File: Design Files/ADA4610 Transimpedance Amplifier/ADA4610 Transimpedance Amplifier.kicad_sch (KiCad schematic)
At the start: 22 parts

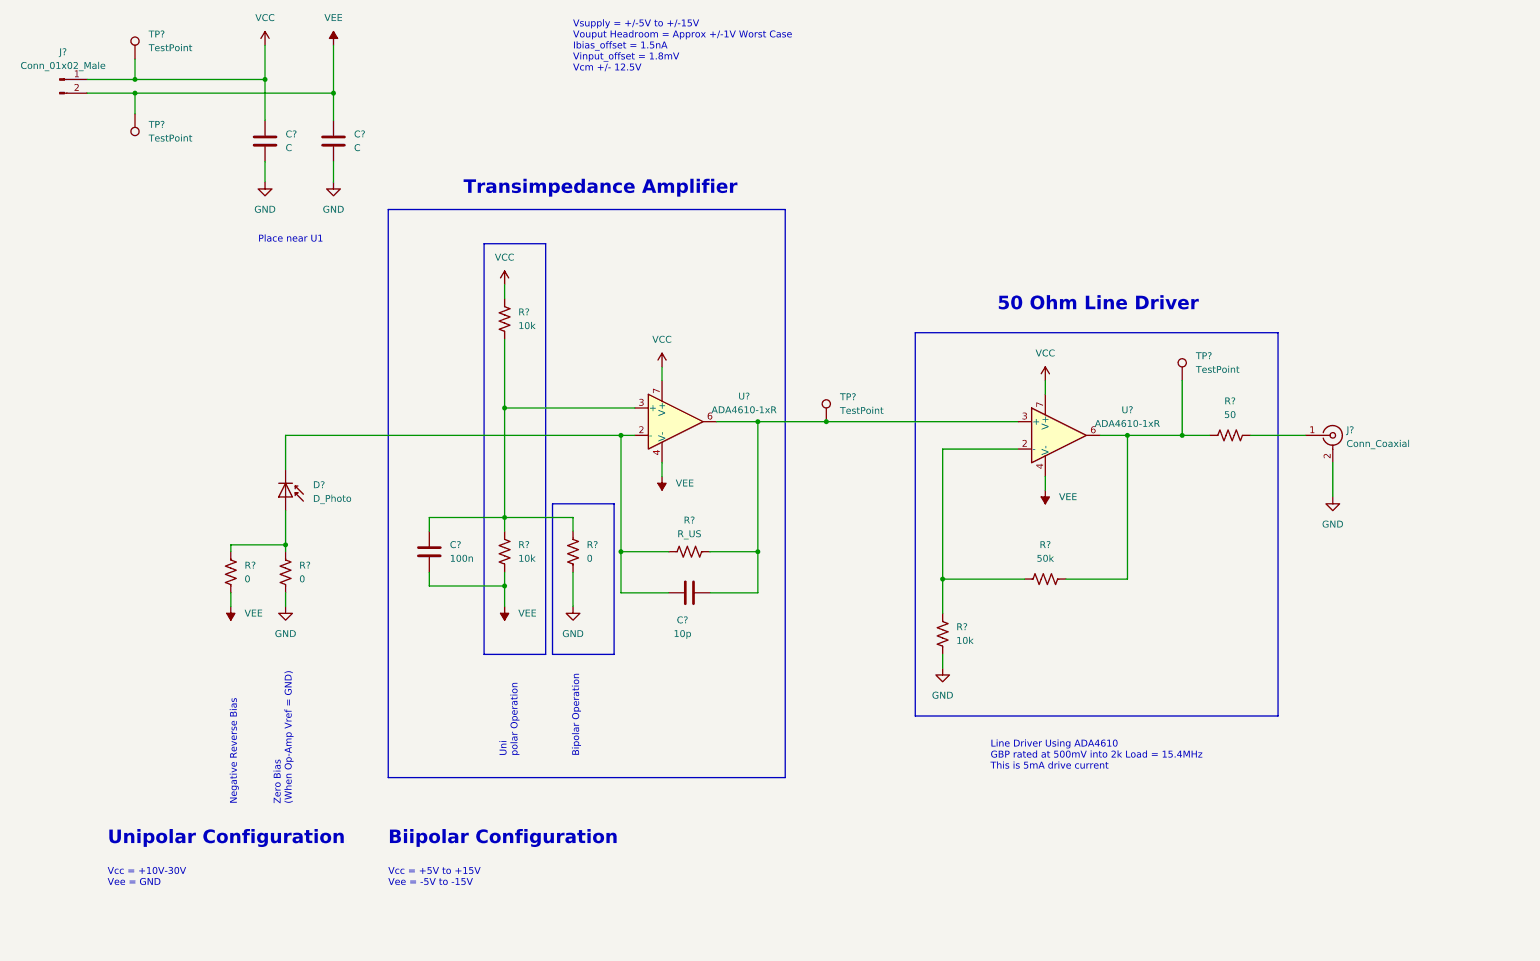
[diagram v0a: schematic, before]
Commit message: Initial pass finished.
Finished the initial schematic and scope. Also did some simulations. Google drive has the dBm output calculations.
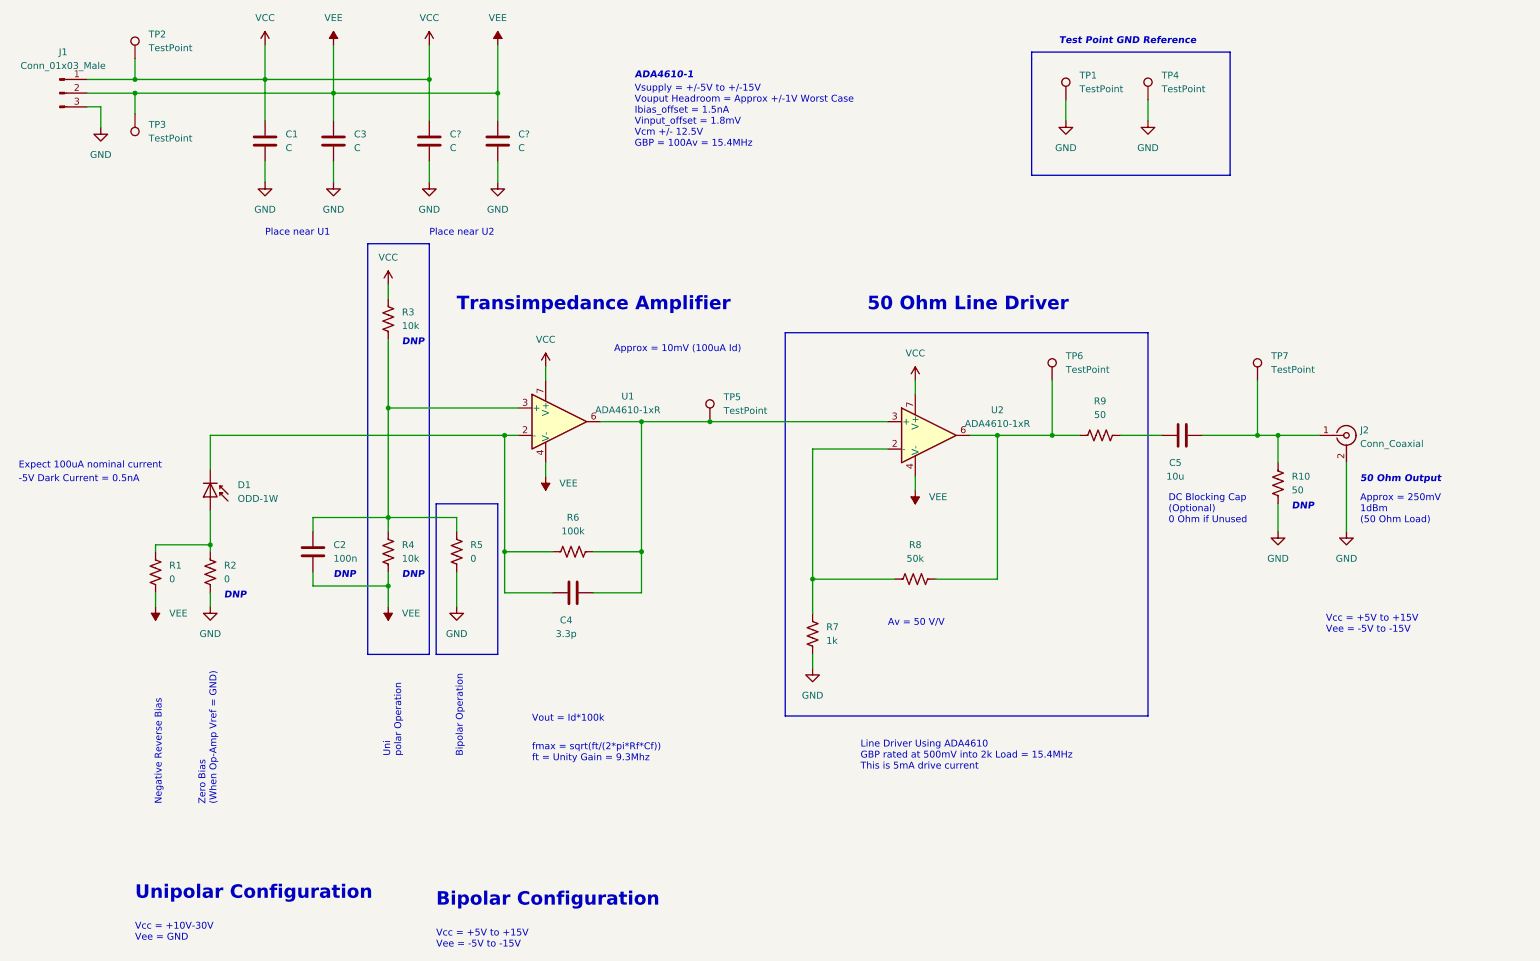
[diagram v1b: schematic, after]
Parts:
- removed J?: Conn_01x02_Male, symbol Connector:Conn_01x02_Male
- added C5: 10u, symbol Device:C
- added C? (x2): C, symbol Device:C
- added J1: Conn_01x03_Male, symbol Connector:Conn_01x03_Male
- added R10: 50, symbol Device:R_US
- added TP1, TP4, TP7: TestPoint, symbol Connector:TestPoint
- C4: renamed from C?; value 10p -> 3.3p
- D1: renamed from D?; value D_Photo -> ODD-1W
- R6: renamed from R?; value R_US -> 100k
- R7: renamed from R?; value 10k -> 1k
- gave numbers to parts that had none: 17
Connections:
- net GND: now also C?.1, C?.1, J1.3 (Pin_3), R10.2, TP1.1, TP4.1
- net VCC: now also C?.2, J1.1 (Pin_1)
- net VEE: now also C?.2, J1.2 (Pin_2)
- net at J2.1 (In): now also C5.2, R10.1, TP7.1; no longer R9.1
- new net: C5.1, R9.1
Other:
- note added: "-5V Dark Current = 0.5nA"
- note added: "50 Ohm Output"
- note added: "ADA4610-1"
- note added: "Approx = 10mV (100uA Id)"
- note added: "Approx = 250mV 1dBm (50 Ohm Load)"
- note added: "Av = 50 V/V"
- note added: "Bipolar Configuration"
- note added: "DC Blocking Cap (Optional) 0 Ohm if Unused"
- note added: "DNP"
- note added: "Expect 100uA nominal current"
- note added: "Place near U2"
- note added: "Test Point GND Reference"
- note added: "Vout = Id*100k"
- note added: "Vsupply = +/-5V to +/-15V Vouput Headroom = Approx +/-1V Worst Case Ibias_offset = 1.5nA Vinput_offset = 1.8mV Vcm +/- 12.5V GBP = 100Av = 15.4MHz"
- note added: "fmax = sqrt(ft/(2*pi*Rf*Cf)) ft = Unity Gain = 9.3Mhz"
- note removed: "Biipolar Configuration"
- note removed: "Vsupply = +/-5V to +/-15V Vouput Headroom = Approx +/-1V Worst Case Ibias_offset = 1.5nA Vinput_offset = 1.8mV Vcm +/- 12.5V"
- company: (none) -> Brenton Salmi, KB1LQD
- title: (none) -> ADA4610-1 Transimpedance Amplifier
- moved on the sheet: C2, C4, D1, J2, R1, R2, R3, R4, R5, R6, R7, R8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

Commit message: Assigned most footprints - picked parts.
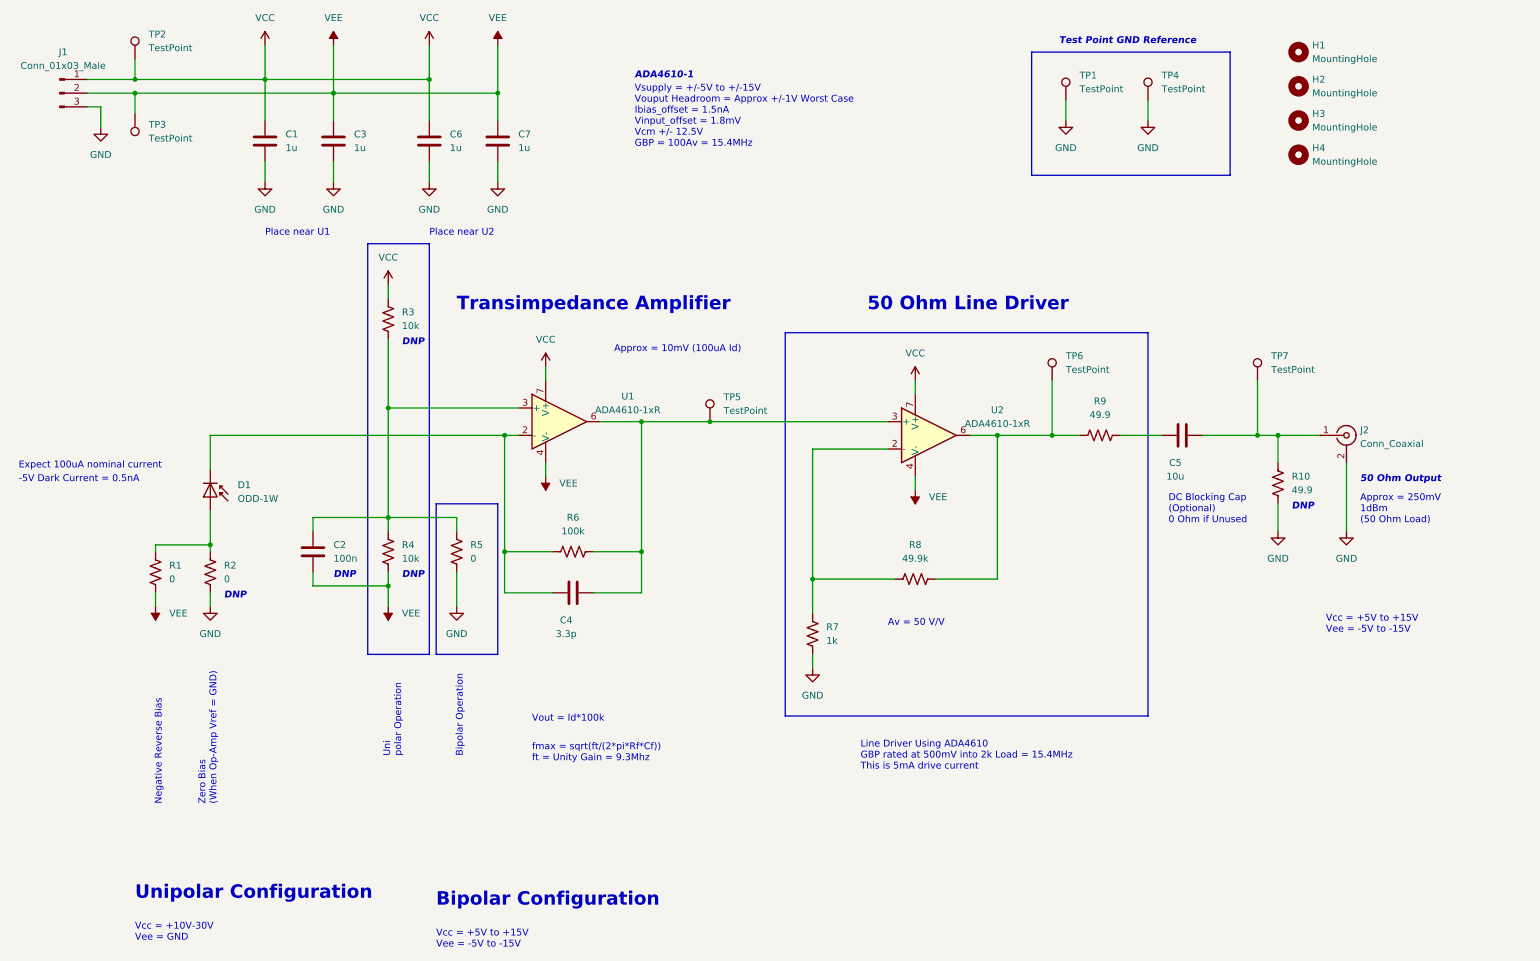
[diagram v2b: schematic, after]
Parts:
- added H1, H2, H3, H4: MountingHole, MountingHole:MountingHole_4.3mm_M4, symbol Mechanical:MountingHole
- C1, C3: value C -> 1u; footprint (none) -> Capacitor_SMD:C_1206_3216Metric_Pad1.33x1.80mm_HandSolder
- C2: footprint (none) -> Capacitor_SMD:C_0805_2012Metric_Pad1.18x1.45mm_HandSolder
- C4: footprint (none) -> Capacitor_SMD:C_0603_1608Metric_Pad1.08x0.95mm_HandSolder
- C5: footprint (none) -> Capacitor_SMD:C_1210_3225Metric_Pad1.33x2.70mm_HandSolder
- C6, C7: renamed from C?; value C -> 1u; footprint (none) -> Capacitor_SMD:C_1206_3216Metric_Pad1.33x1.80mm_HandSolder
- J1: footprint (none) -> Connector_Molex:Molex_KK-254_AE-6410-03A_1x03_P2.54mm_Vertical
- R1, R2, R3, R4, R5, R7: footprint (none) -> Resistor_SMD:R_0603_1608Metric_Pad0.98x0.95mm_HandSolder
- R10, R9: value 50 -> 49.9; footprint (none) -> Resistor_SMD:R_0805_2012Metric_Pad1.20x1.40mm_HandSolder
- R6: footprint (none) -> Resistor_SMD:R_0805_2012Metric_Pad1.20x1.40mm_HandSolder
- R8: value 50k -> 49.9k; footprint (none) -> Resistor_SMD:R_0805_2012Metric_Pad1.20x1.40mm_HandSolder
- TP1, TP2, TP3, TP4, TP5, TP6, TP7: footprint (none) -> TestPoint:TestPoint_Keystone_5010-5014_Multipurpose
- U1, U2: footprint Package_SO:SOIC-8_3.9x4.9mm_P1.27mm -> Package_TO_SOT_SMD:SOT-23-5_HandSoldering

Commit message: All components and footprints assigned and created. Layout imported parts.
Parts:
- D1: footprint (none) -> Package_TO_SOT_THT:TO-18-2_Lens
- J2: footprint (none) -> ADA4610-transimpedance-amplifier:RFSOLUTIONS_CON-SMA-EDGE-S
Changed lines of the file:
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@@
       (effects (font (size 1.27 1.27)) (justify left))
     )
-    (property "Footprint" "" (id 2) (at 50.8 105.41 0)
+    (property "Footprint" "Package_TO_SOT_THT:TO-18-2_Lens" (id 2) (at 50.8 105.41 0)
       (effects (font (size 1.27 1.27)) hide)
     )
@@
       (effects (font (size 1.27 1.27)) (justify left))
     )
-    (property "Footprint" "" (id 2) (at 261.62 95.25 0)
+    (property "Footprint" "ADA4610-transimpedance-amplifier:RFSOLUTIONS_CON-SMA-EDGE-S" (id 2) (at 261.62 95.25 0)
       (effects (font (size 1.27 1.27)) hide)
     )
@@
     )
     (path "/77fe5954-2f88-4ed4-92bc-bc3cc4ac221b"
-      (reference "D1") (unit 1) (value "ODD-1W") (footprint "")
+      (reference "D1") (unit 1) (value "ODD-1W") (footprint "Package_TO_SOT_THT:TO-18-2_Lens")
     )
     (path "/0e9ad7f4-e2e4-4f66-a3cd-b654f2049983"
@@
     )
     (path "/95f2c62c-a009-4fa4-97f8-20f682525c95"
-      (reference "J2") (unit 1) (value "Conn_Coaxial") (footprint "")
+      (reference "J2") (unit 1) (value "Conn_Coaxial") (footprint "ADA4610-transimpedance-amplifier:RFSOLUTIONS_CON-SMA-EDGE-S")
     )
     (path "/713ca44b-f876-4e30-93a9-006e69ad0296"
